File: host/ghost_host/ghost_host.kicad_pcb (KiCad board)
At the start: 2 copper layers, 127.5 x 68.5 mm, 117 parts, among them J1 RGB_3_Pin_Connector, J10 Conn_01x06, J11 Conn_01x04, J12 RJ12_Shielded, J13 Conn_01x06, J14 Conn_01x04, J15 RJ12_Shielded, J16 Conn_01x06, J17 Conn_01x04, J18 RJ12_Shielded, J19 Conn_01x06, J2 Conn_01x04, J20 Conn_01x04, J21 RJ12_Shielded, J22 Conn_01x06, J23 RJ12_Shielded, J24 Conn_01x06, J25 Conn_01x06, J3 Conn_01x04, J4 RJ12_Shielded, J5 Conn_01x04, J6 RJ12_Shielded, J7 Conn_01x06, J8 Conn_01x04, J9 RJ12_Shielded, U1 PCA9615DP, U2 PCA9615DP, U3 PCA9615DP, U4 PCA9615DP, U5 PCA9615DP, U6 PCA9615DP, U7 PCA9615DP, U8 PCA9615DP, U9 kb2040

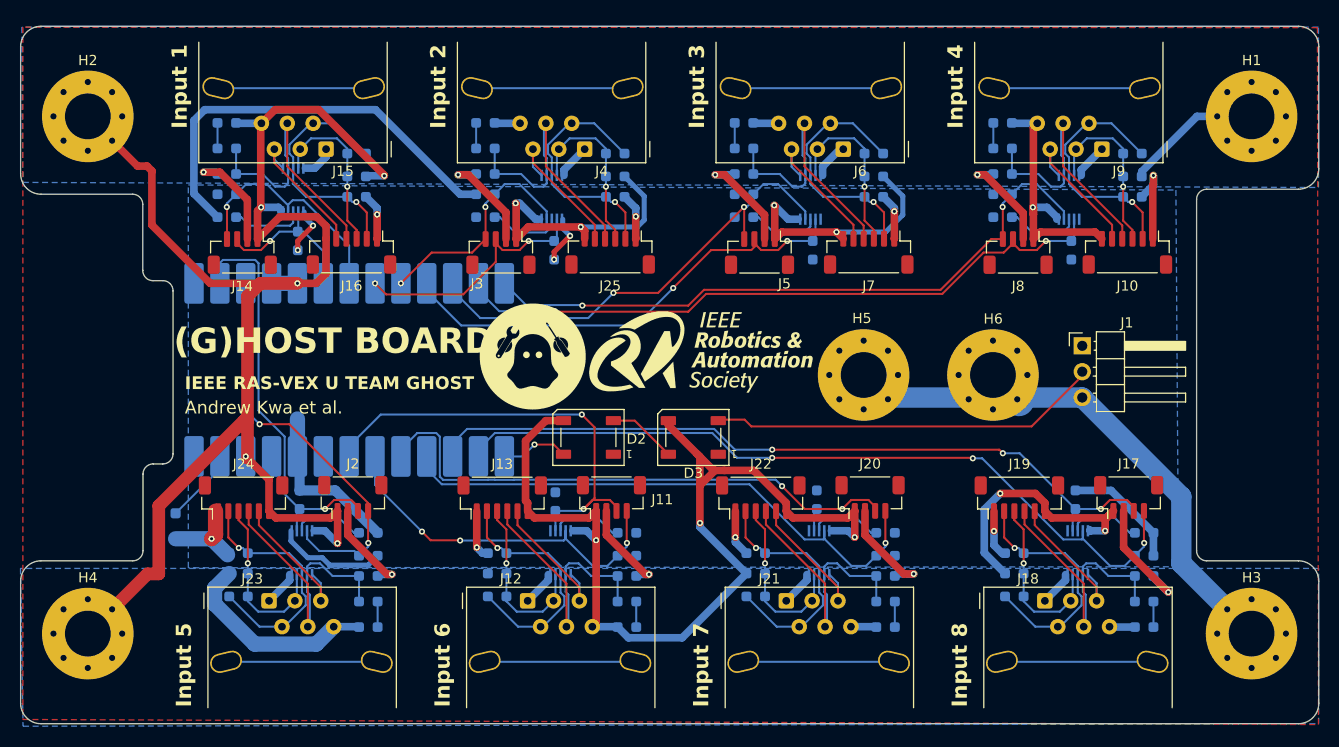
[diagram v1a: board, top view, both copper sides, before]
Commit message: add caps to host; make sensor_breakouts larger; update bom & generated production files for everything
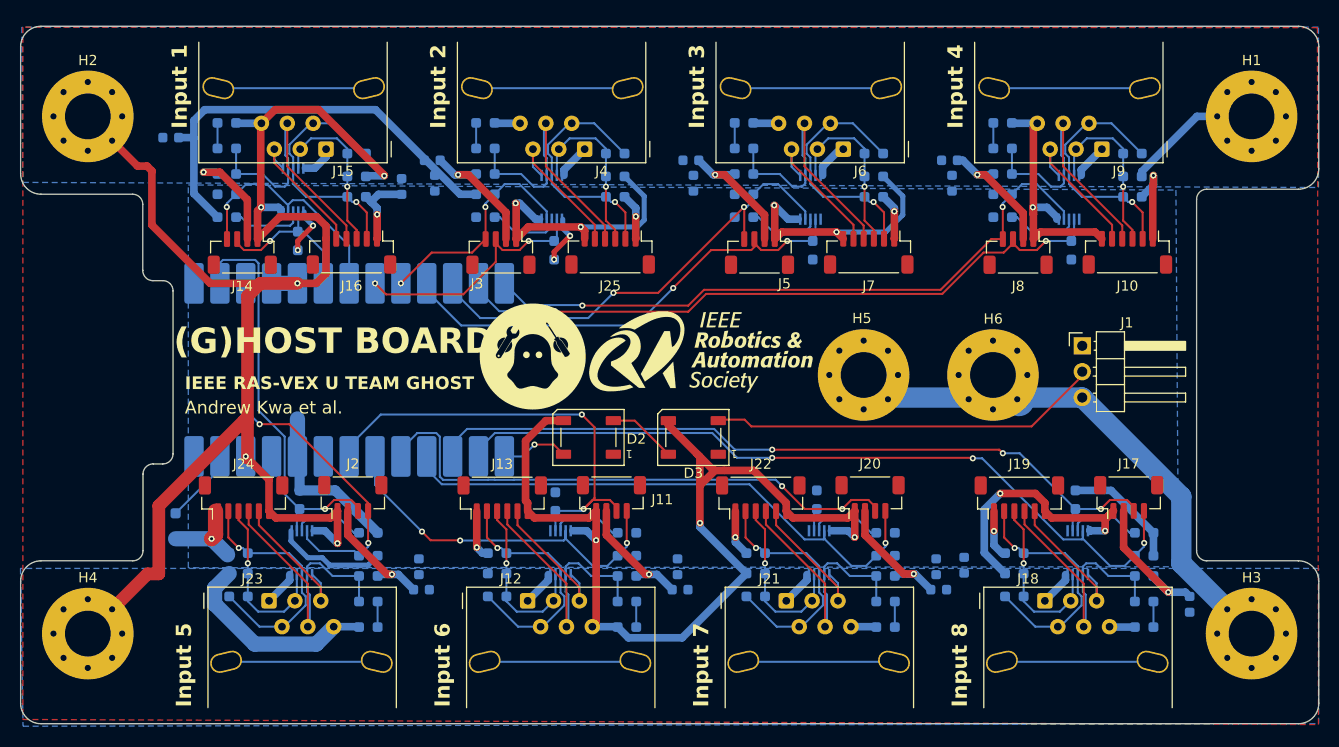
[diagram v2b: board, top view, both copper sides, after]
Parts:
- added C1: 1u, Capacitor_SMD:C_0603_1608Metric, B.Cu at (119.4, 107.0)
- added C10: 1u, Capacitor_SMD:C_0603_1608Metric, B.Cu at (120.7, 67.1)
- added C11: 1u, Capacitor_SMD:C_0603_1608Metric, B.Cu at (146.1, 67.1)
- added C12: 1u, Capacitor_SMD:C_0603_1608Metric, B.Cu at (171.5, 67.1)
- added C13: 1u, Capacitor_SMD:C_0603_1608Metric, B.Cu at (145.1, 109.2)
- added C14: 1u, Capacitor_SMD:C_0603_1608Metric, B.Cu at (117.7, 69.7)
- added C15: 1u, Capacitor_SMD:C_0603_1608Metric, B.Cu at (195.1, 110.7)
- added C16: 1u, Capacitor_SMD:C_0603_1608Metric, B.Cu at (170.4, 109.2)
- added C2: 1u, Capacitor_SMD:C_0603_1608Metric, B.Cu at (121.0, 69.3)
- added C3: 1u, Capacitor_SMD:C_0603_1608Metric, B.Cu at (146.4, 69.3)
- added C4: 1u, Capacitor_SMD:C_0603_1608Metric, B.Cu at (171.8, 69.3)
- added C5: 1u, Capacitor_SMD:C_0603_1608Metric, B.Cu at (144.8, 107.0)
- added C6: 1u, Capacitor_SMD:C_0603_1608Metric, B.Cu at (95.0, 64.8)
- added C7: 1u, Capacitor_SMD:C_0603_1608Metric, B.Cu at (172.9, 106.8)
- added C8: 1u, Capacitor_SMD:C_0603_1608Metric, B.Cu at (170.2, 107.0)
- added C9: 1u, Capacitor_SMD:C_0603_1608Metric, B.Cu at (119.7, 109.2)
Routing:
- net +5V: track 157.1 -> 177.8 mm
- net +3.3V: track 90.7 -> 92.2 mm
